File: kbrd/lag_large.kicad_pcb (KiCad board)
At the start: 2 copper layers, 166.7 x 137.4 mm, 73 parts

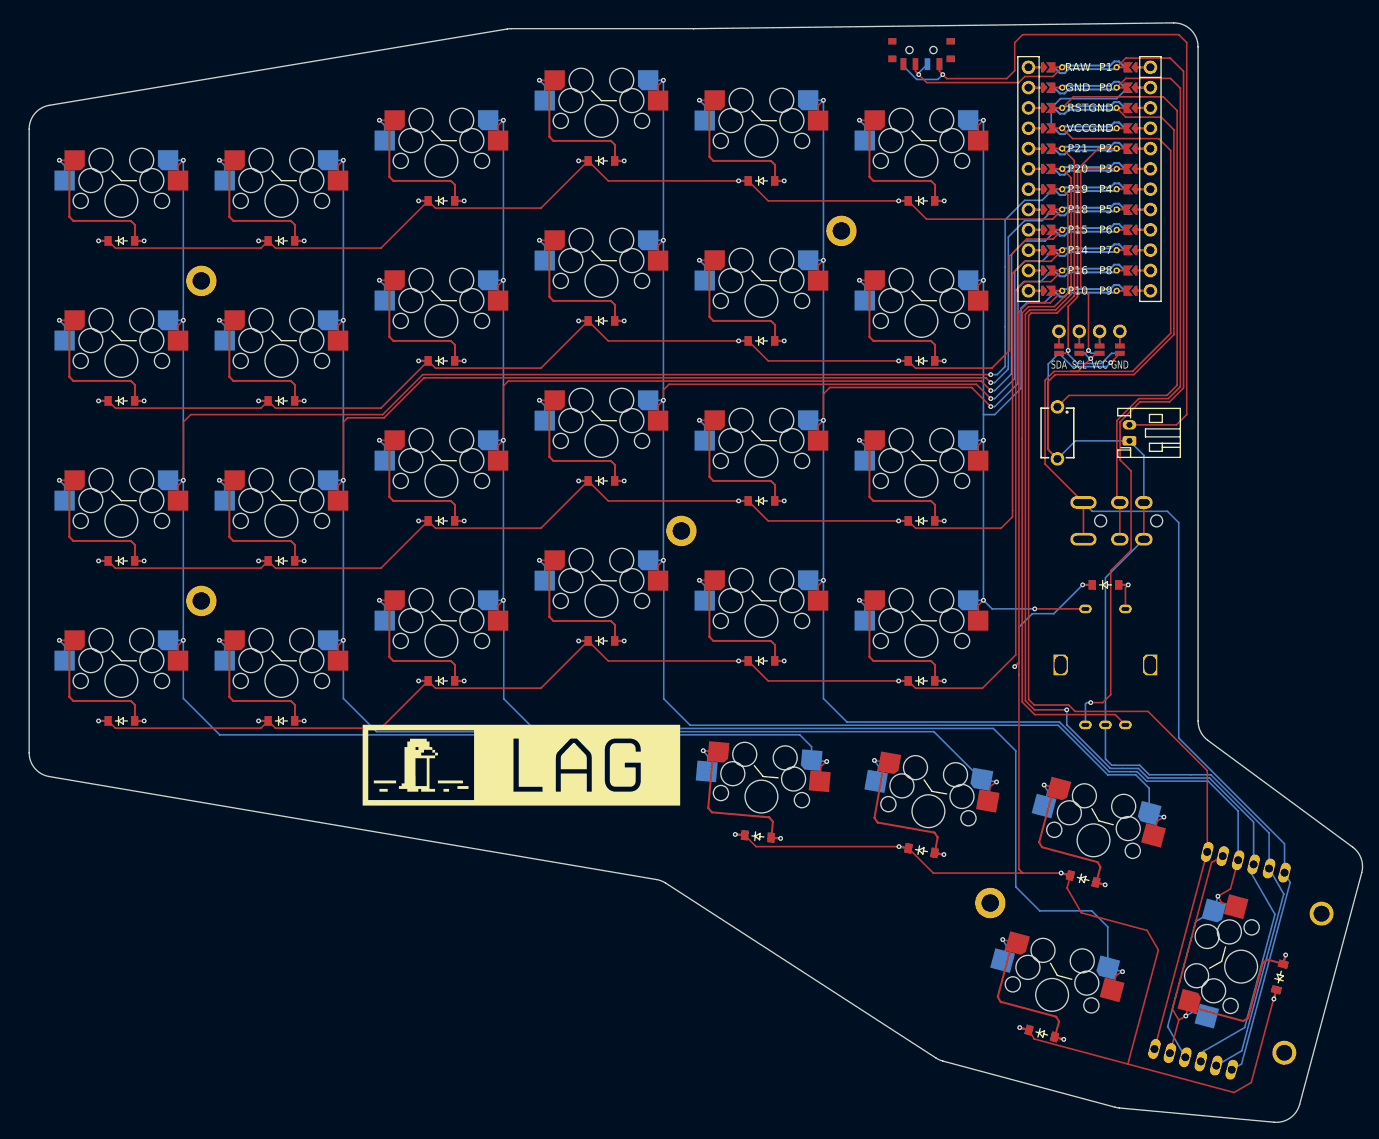
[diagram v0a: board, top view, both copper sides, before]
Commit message: changes in routes and add gerber files
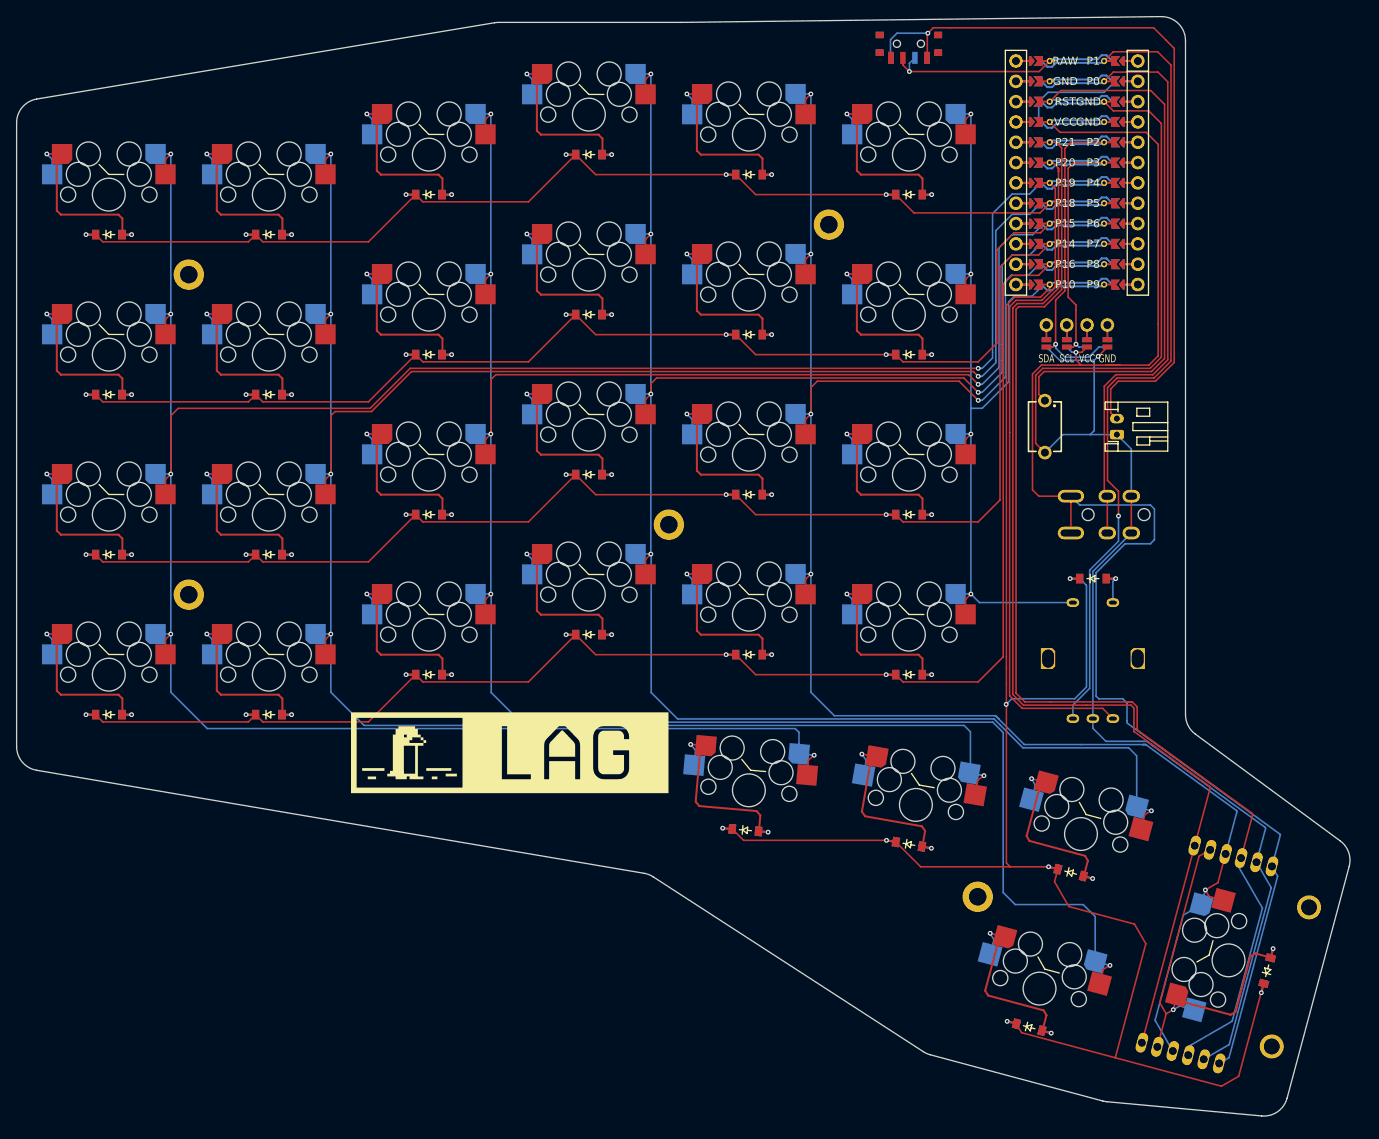
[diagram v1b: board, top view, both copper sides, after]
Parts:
- moved D13 1.75 mm to (127.3, 135.0)
- moved D20 1.75 mm to (147.3, 77.5)
- moved RE1 1.75 mm to (190.3, 138.0)
- moved S19 1.75 mm to (147.3, 92.5)
- moved D24 1.75 mm to (167.3, 80.0)
- moved D30 1.75 mm to (190.3, 128.0)
- moved S4 1.75 mm to (67.3, 80.0)
- moved H4 1.75 mm to (137.3, 121.3)
- moved S25 1.75 mm to (147.3, 154.5)
- moved S13 1.75 mm to (127.3, 130.0)
- moved XX1 1.75 mm to (212.6, 186.5)
- moved S7 1.75 mm to (87.3, 100.0)
- moved DISP1 1.75 mm to (188.3, 113.0)
- moved D19 1.75 mm to (147.3, 97.5)
- moved S10 1.75 mm to (107.3, 115.0)
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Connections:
- XX1 pad 3: P20 -> P21
- XX1 pad 6: P21 -> P20
- XX2 pad 3: P20 -> P21
- XX2 pad 6: P21 -> P20
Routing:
- net VCC: track 182.4 -> 199.4 mm
- net P21: track 145.3 -> 156.0 mm
- net P10: track 229.1 -> 238.2 mm
- net P20: track 151.2 -> 145.3 mm, vias 1 -> 0
- net GND: track 237.3 -> 233.2 mm
- net P5: track 301.8 -> 305.0 mm
- net P6: track 301.6 -> 303.7 mm
- net P7: track 245.7 -> 247.6 mm
- net sw1: track 97.2 -> 95.5 mm
- net P8: track 245.5 -> 246.8 mm
- net RST: track 75.9 -> 77.2 mm
- net P2: track 48.2 -> 49.2 mm
- net P14: track 184.5 -> 183.8 mm
- net P1: track 110.6 -> 110.0 mm
- net P16: track 200.6 -> 201.2 mm
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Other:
- board text added: "DON'T PANIC"
- board text added: "SERENITY NOW!"
- board text added: "msjtw 2025"
- board text removed: "LAG 2025"
